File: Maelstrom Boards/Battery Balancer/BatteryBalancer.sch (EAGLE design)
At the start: 18 parts, among them P1 39-30-06, P2 39-30-06, P3 39-30-06, P4 39-30-08, P5 39-30-08, P6 39-30-02

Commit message: File Directory changed
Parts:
- removed P3: 39-30-06, con-molex-mini-fit:39-30-06
- removed P4, P5: 39-30-08, con-molex-mini-fit:39-30-08
- added C1: (no value), rcl:C-EUC0603
- added C2: (no value), rcl:CPOL-USE2-4
- added R1, R2, R3, R4: 100K, rcl:R-US_R0603
- P1: value 39-30-06 -> 39-30-14; device con-molex-mini-fit:39-30-06 -> con-molex-mini-fit:39-30-14
- P6: value 39-30-02 -> 39-30-16; device con-molex-mini-fit:39-30-02 -> con-molex-mini-fit:39-30-16
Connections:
- removed net MOTOR_POWER1: P5.1, P5.2, P5.3, P5.4, U$8.LOAD-, U$9.LOAD-
- new net GNDA: C1.2, C2.-, R3.2, R4.2, U$12.GND
- new net MOTOR_POWER: P1.1, P1.2, P1.3, P1.4, P1.5, P1.6, P1.7, U$8.LOAD-, U$9.LOAD-
- new net N$7: R1.2, R3.1, U$12.A0
- new net N$8: R1.1, R2.1, R2.2, R4.1, U$12.A1, U$12.V+
- net +3V3: now also C1.1, C2.+, U$12.VREF
- net BALANCED_OUT: now also P2.1, P2.2, P2.3; no longer P3.1, P3.2, P3.3
- net GND: now also P1.10, P1.11, P1.12, P1.13, P1.14, P1.8, P1.9, P6.10, P6.11, P6.12, P6.13, P6.14, P6.15, P6.16, P6.9; no longer P1.4, P1.5, P1.6, P3.4, P3.5, P3.6, P4.5, P4.6, P4.7, P4.8, P5.5, P5.6, P5.7, P5.8
- net KILL_SWITCH: no longer P6.1
- net MOTOR_POWER2: no longer P4.1, P4.2, P4.3, P4.4
- net PORT_BATTERY: now also P6.5, P6.6, P6.7, P6.8; no longer P1.1, P1.2, P1.3
- net STBD_BATTERY: now also P6.1, P6.2, P6.3, P6.4; no longer P2.1, P2.2, P2.3

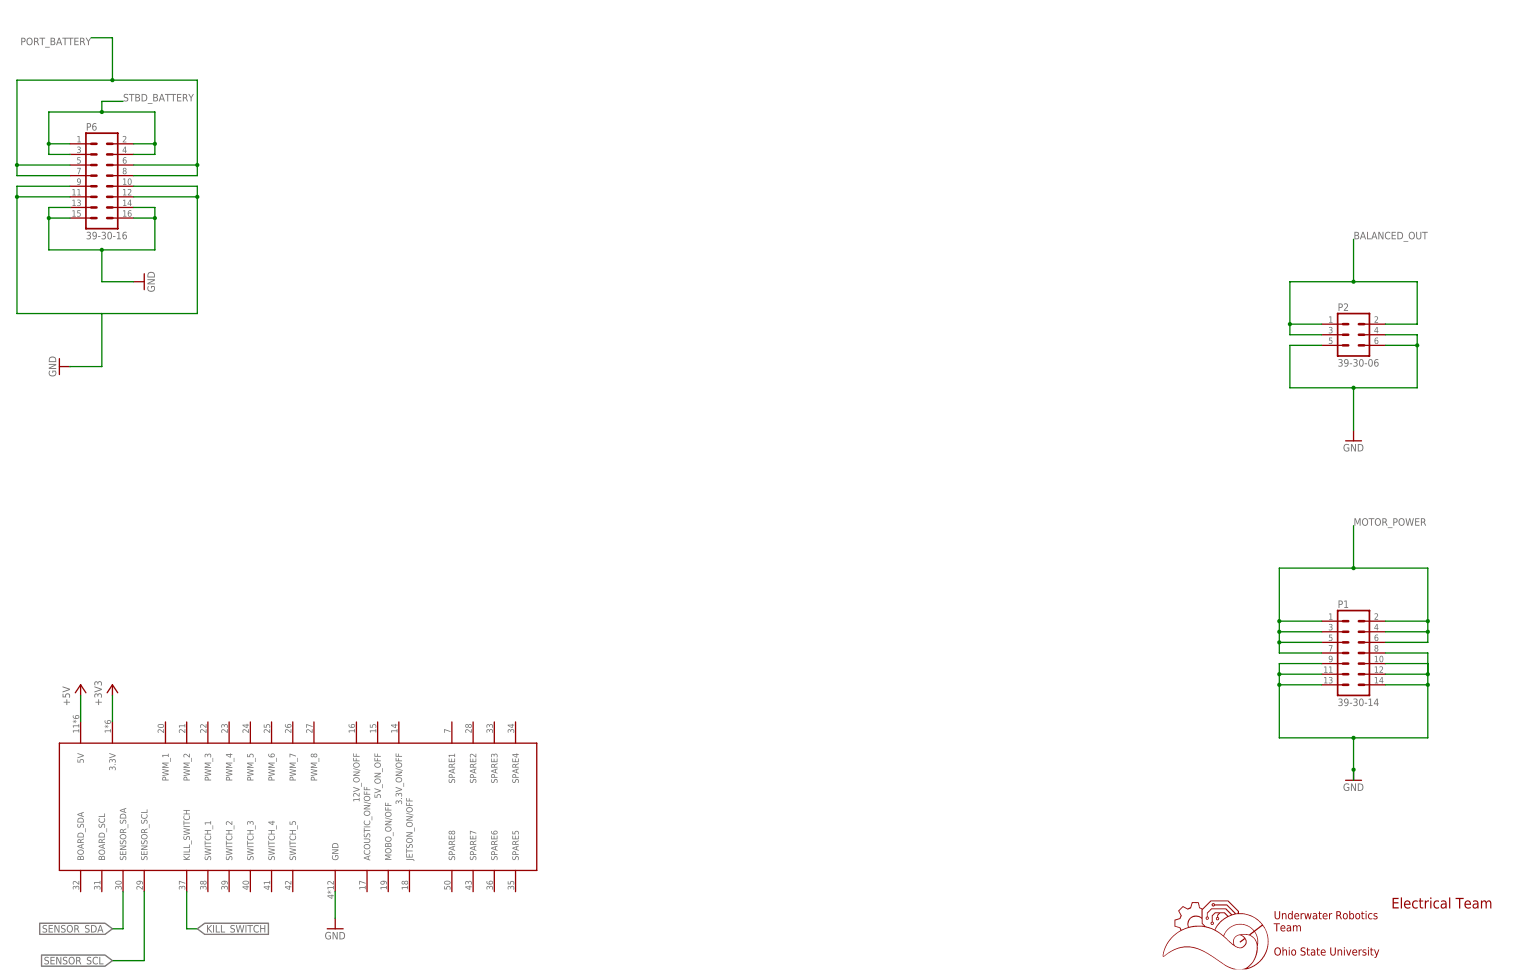
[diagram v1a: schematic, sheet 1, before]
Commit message: updated battery balancer
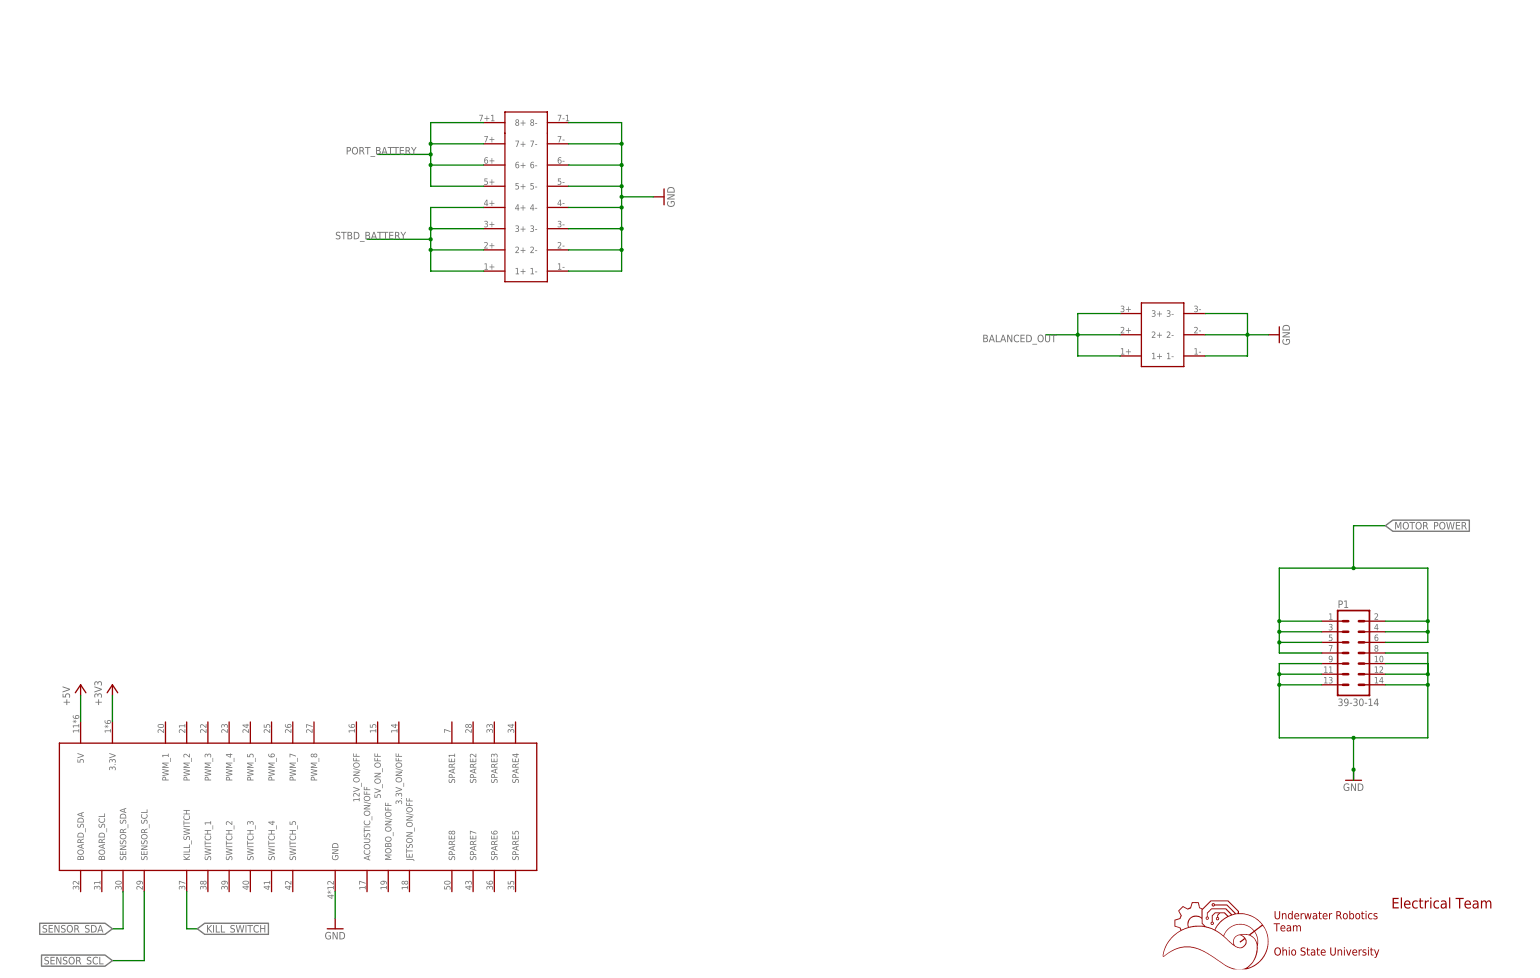
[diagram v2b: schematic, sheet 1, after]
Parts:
- removed C2: (no value), rcl:CPOL-USE2-4
- removed P2: 39-30-06, con-molex-mini-fit:39-30-06
- removed P6: 39-30-16, con-molex-mini-fit:39-30-16
- added BALANCED_LED, KILLSWITCH_LED, PORT_LED, STBD_LED: (no value), led:LEDCHIP-LED0603
- added R10, R6, R8: 400, rcl:R-US_R0603
- added R11, R12, R13, R14: 1450, rcl:R-US_R0603
- added R5, R7, R9: 2.6k, rcl:R-US_R0603
- added U$13: 6PIN-VERT, Vertical_Connectors:6PIN-VERT
- added U$14: 16PIN-VERT, Vertical_Connectors:16PIN-VERT
- C1: value (none) -> 0.1uF
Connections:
- removed net LOAD: U$10.LOAD+, U$11.LOAD+, U$8.LOAD+, U$9.LOAD+
- removed net MOTOR_POWER2: U$10.LOAD-, U$11.LOAD-
- new net N$10: R8.2, R9.2, U$12.IN4
- new net N$11: PORT_LED.A, R11.2
- new net N$12: R12.2, STBD_LED.A
- new net N$13: BALANCED_LED.A, R13.1
- new net N$14: KILLSWITCH_LED.A, R14.1
- new net N$15: R5.2, R6.2, U$12.IN2
- new net N$6: R2.2, R4.1, U$12.A1
- new net N$9: R10.2, R7.2, U$12.IN3
- net +3V3: no longer C2.+
- net BALANCED_OUT: now also R13.2, R5.1, U$10.LOAD+, U$11.LOAD+, U$13.1+, U$13.2+, U$13.3+, U$8.LOAD+, U$9.LOAD+; no longer P2.1, P2.2, P2.3
- net GND: now also BALANCED_LED.C, KILLSWITCH_LED.C, PORT_LED.C, STBD_LED.C, U$13.1-, U$13.2-, U$13.3-, U$14.1-, U$14.2-, U$14.3-, U$14.4-, U$14.5-, U$14.6-, U$14.7-, U$14.8-; no longer P2.4, P2.5, P2.6, P6.10, P6.11, P6.12, P6.13, P6.14, P6.15, P6.16, P6.9
- net GNDA: now also R10.1, R6.1, R8.1; no longer C2.-
- net KILL_SWITCH: now also R14.2
- net MOTOR_POWER: now also U$10.LOAD-, U$11.LOAD-
- net N$8: no longer R2.2, R4.1, U$12.A1
- net PORT_BATTERY: now also R11.1, R7.1, U$14.5+, U$14.6+, U$14.7+, U$14.8+; no longer P6.5, P6.6, P6.7, P6.8
- net STBD_BATTERY: now also R12.1, R9.1, U$14.1+, U$14.2+, U$14.3+, U$14.4+; no longer P6.1, P6.2, P6.3, P6.4
- net STBD_CURRENT: now also U$12.IN1; no longer U$12.IN3

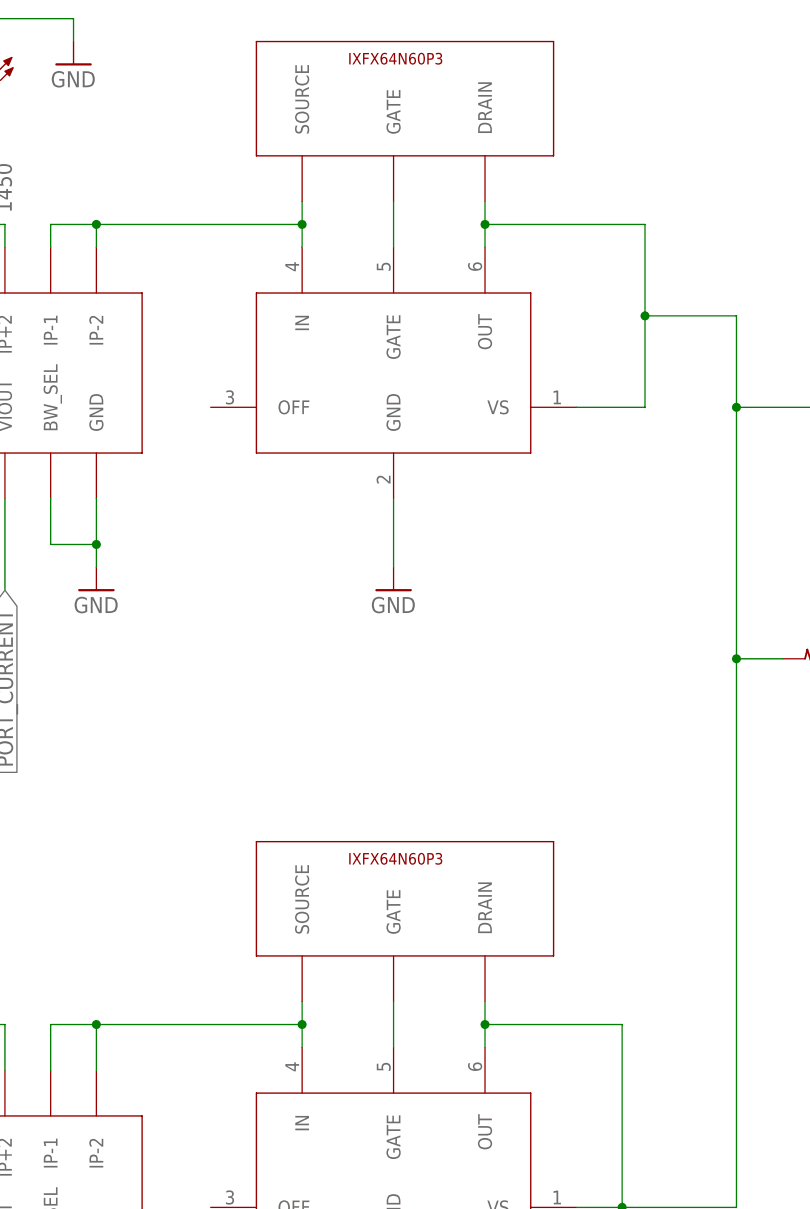
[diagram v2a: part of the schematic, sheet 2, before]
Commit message: changed MOSFET
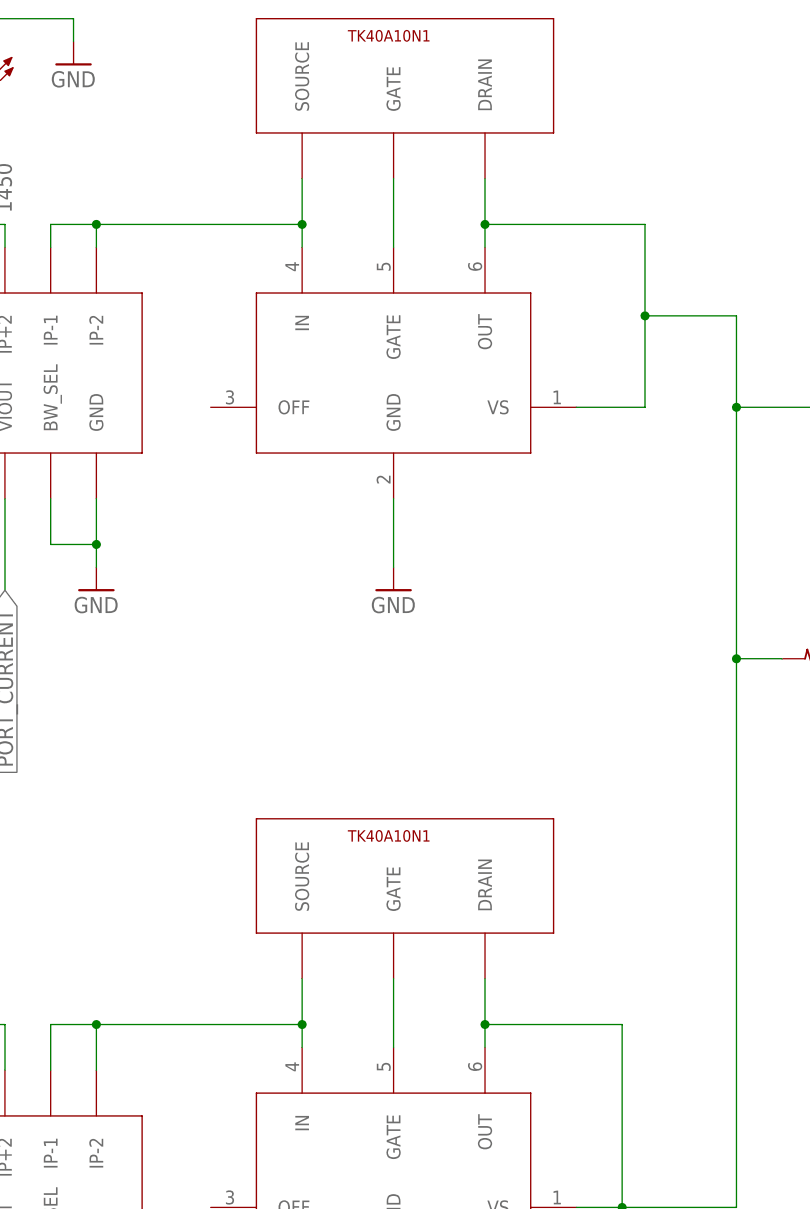
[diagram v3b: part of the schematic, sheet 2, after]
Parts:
- removed U$4: IXFX64N60P3, IXFX64N60P3:IXFX64N60P3
- added U$15: IXFX64N60P3TK40A10N1, TK40A10N1:IXFX64N60P3TK40A10N1
- U$5: value IXFX64N60P3 -> IXFX64N60P3TK40A10N1; device IXFX64N60P3:IXFX64N60P3 -> TK40A10N1:IXFX64N60P3TK40A10N1
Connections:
- net BALANCED_OUT: now also U$15.DRAIN; no longer U$4.DRAIN
- net N$1: now also U$15.SOURCE; no longer U$4.SOURCE
- net N$2: now also U$15.GATE; no longer U$4.GATE

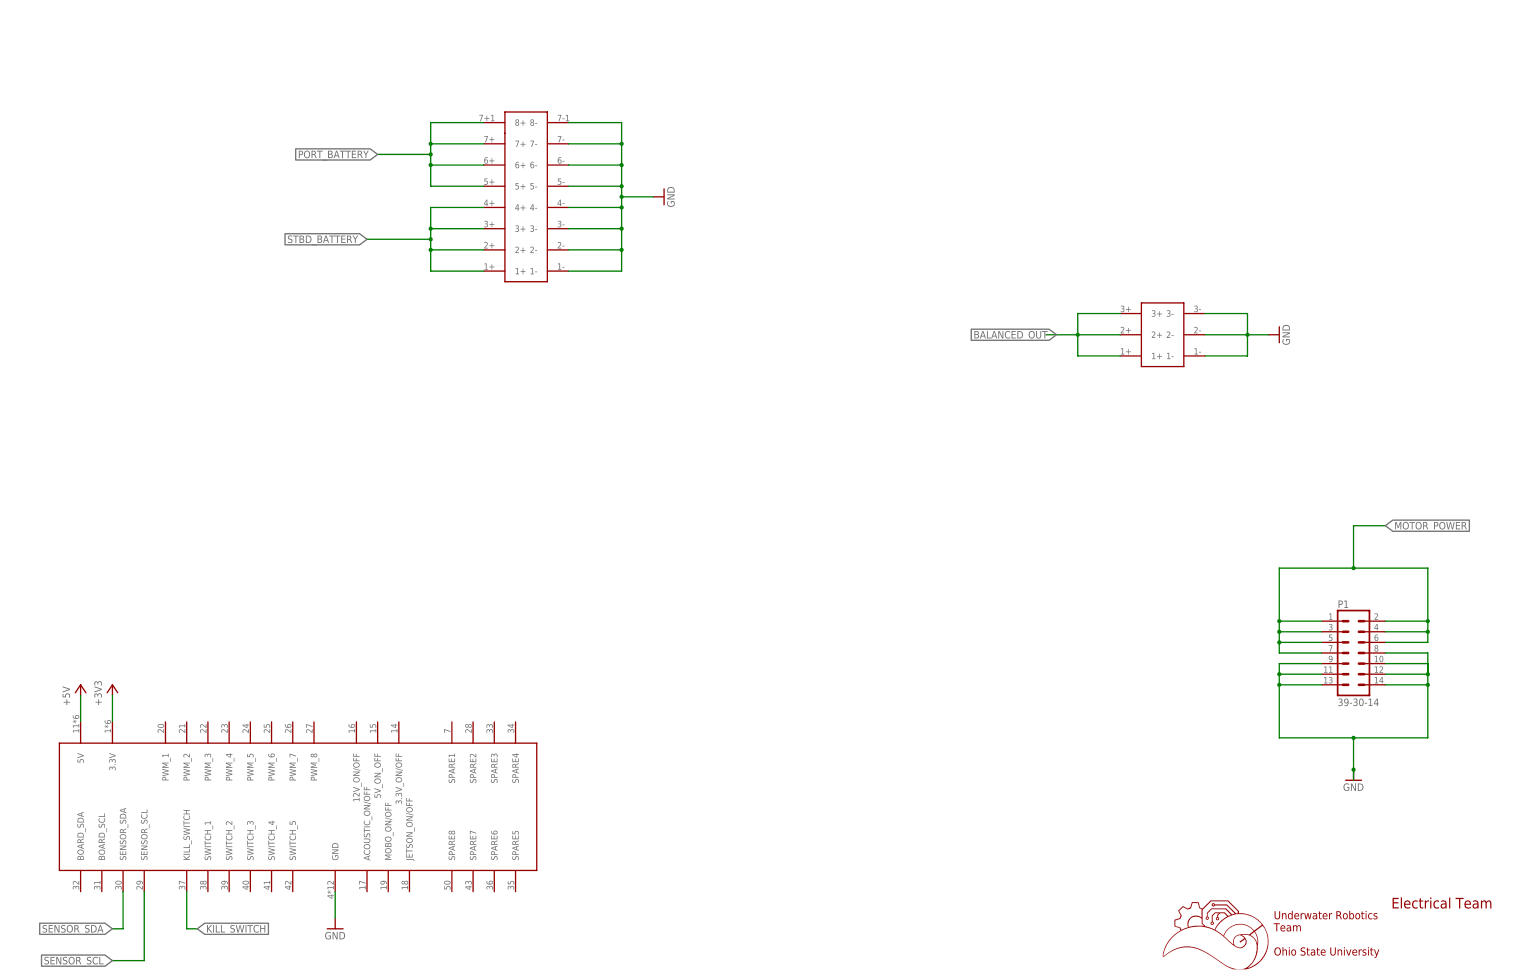
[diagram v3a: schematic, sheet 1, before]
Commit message: Completed Battery Balancer
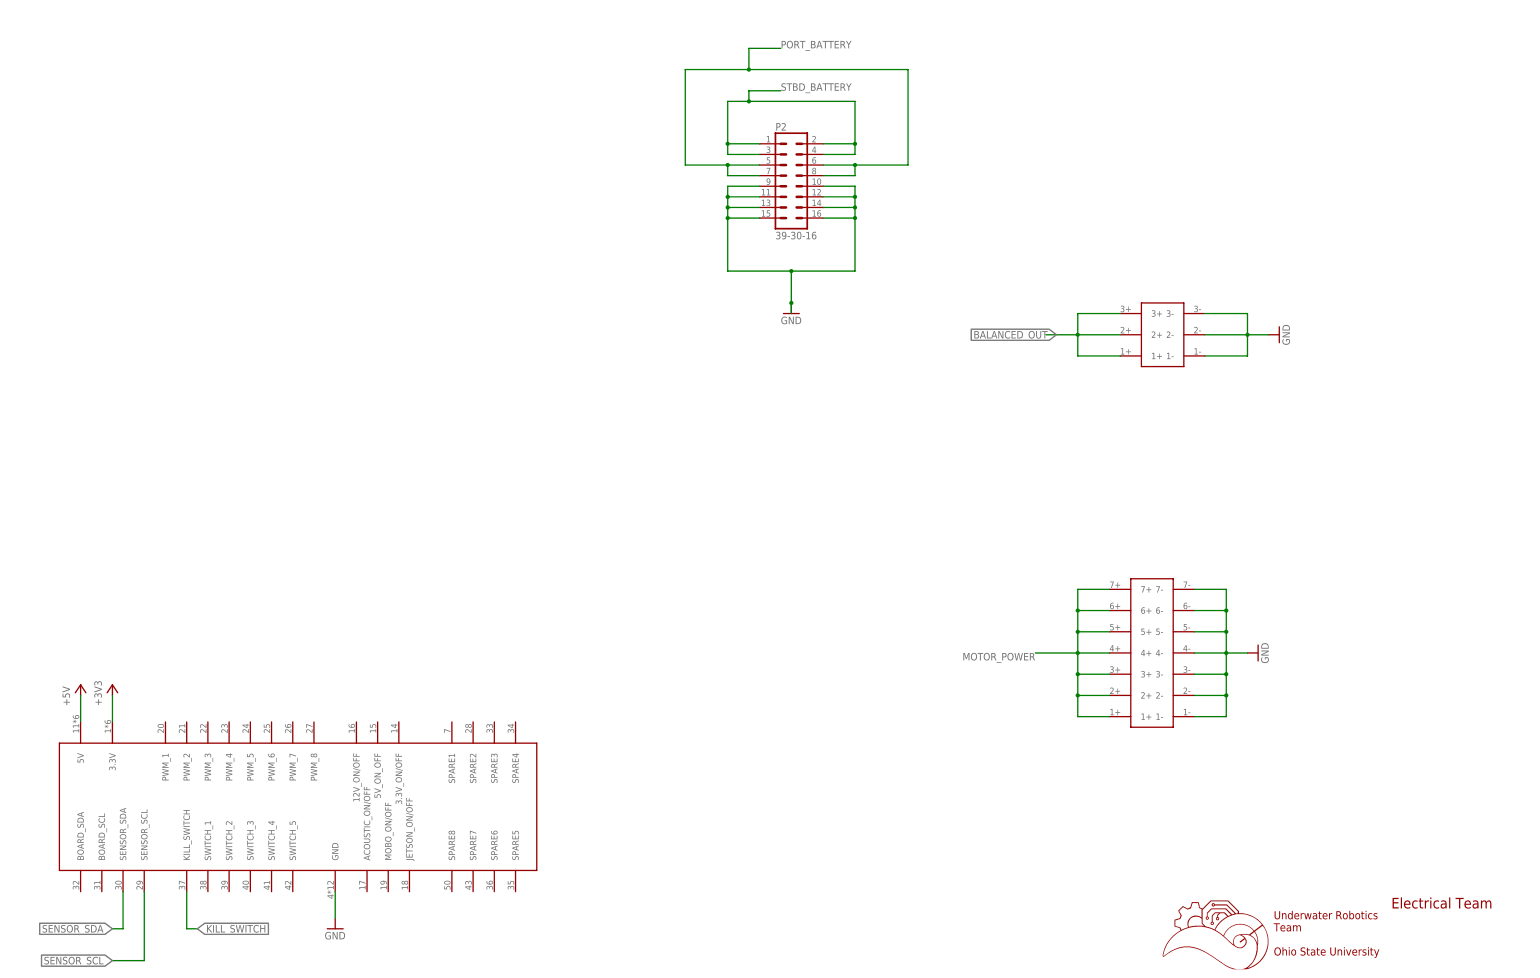
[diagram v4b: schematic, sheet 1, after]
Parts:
- removed P1: 39-30-14, con-molex-mini-fit:39-30-14
- removed U$14: 16PIN-VERT, Vertical_Connectors:16PIN-VERT
- added P2: 39-30-16, con-molex-mini-fit:39-30-16
- added U$4: 14PIN-VERT, Vertical_Connectors:14PIN-VERT
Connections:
- net GND: now also P2.10, P2.11, P2.12, P2.13, P2.14, P2.15, P2.16, P2.9, U$4.1-, U$4.2-, U$4.3-, U$4.4-, U$4.5-, U$4.6-, U$4.7-; no longer P1.10, P1.11, P1.12, P1.13, P1.14, P1.8, P1.9, U$14.1-, U$14.2-, U$14.3-, U$14.4-, U$14.5-, U$14.6-, U$14.7-, U$14.8-
- net MOTOR_POWER: now also U$4.1+, U$4.2+, U$4.3+, U$4.4+, U$4.5+, U$4.6+, U$4.7+; no longer P1.1, P1.2, P1.3, P1.4, P1.5, P1.6, P1.7
- net PORT_BATTERY: now also P2.5, P2.6, P2.7, P2.8; no longer U$14.5+, U$14.6+, U$14.7+, U$14.8+
- net STBD_BATTERY: now also P2.1, P2.2, P2.3, P2.4; no longer U$14.1+, U$14.2+, U$14.3+, U$14.4+

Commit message: Finalized and updated Battery Balancer Board
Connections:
- net N$4 renamed SOURCE

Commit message: Finalized Battery Balancer
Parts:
- removed U$10, U$11, U$8, U$9: CMX60D20, CMX60D20:CMX60D20
- added Q1: SPB80P06P, transistor-fet:SPB80P06P
- added Q4: 310mA/60V/1.6Ω, SparkFun-DiscreteSemi:MOSFET-NCH-2N7002PW
- added R15, R16: 10K, rcl:R-US_R0603
- R14: value 1450 -> 10K
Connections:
- new net N$16: KILLSWITCH_LED.C, R16.1
- new net N$4: Q4.D, R14.1
- net +3V3: now also KILLSWITCH_LED.A, Q4.G
- net BALANCED_OUT: now also Q1.S, R15.2; no longer U$10.LOAD+, U$11.LOAD+, U$8.LOAD+, U$9.LOAD+
- net GND: no longer KILLSWITCH_LED.C, U$10.CONTROL-, U$11.CONTROL-, U$8.CONTROL-, U$9.CONTROL-
- net KILL_SWITCH: now also Q4.S, R16.2; no longer R14.2, U$10.CONTROL+, U$11.CONTROL+, U$8.CONTROL+, U$9.CONTROL+
- net MOTOR_POWER: now also Q1.D; no longer U$10.LOAD-, U$11.LOAD-, U$8.LOAD-, U$9.LOAD-
- net N$14: now also Q1.G, R14.2, R15.1; no longer KILLSWITCH_LED.A, R14.1
